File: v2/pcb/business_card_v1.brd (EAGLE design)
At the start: 89 x 51 mm, 70 parts, among them SW1 SPST_TACT-KMR2

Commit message: business card
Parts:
- moved U$1 0.90 mm to (5.08, 46.4)
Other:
- board text added: "Website: https://kevin.lutzer.ca Email: kevin@lutzer.ca Github: https://github.com/kevinlutzer Linkedin: www.linkedin.com/in/kevin-lutzer"
- board text removed: "Website: https://kevin.lutzer.ca Email: kevin@lutzer.ca Github: https://github.com/kevinlutzer"
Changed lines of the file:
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@@
 <dimension x1="0" y1="51.79" x2="89" y2="51.79" x3="44.5" y3="56.79" textsize="1" layer="1"/>
 <dimension x1="89" y1="51.79" x2="89" y2="0.79" x3="94" y3="26.29" textsize="1" layer="1"/>
-<text x="8.89" y="47.625" size="1.778" layer="121">v2</text>
-<text x="8.89" y="45.085" size="1.778" layer="121">Kevin Lutzer</text>
-<text x="1.905" y="40.005" size="1.778" layer="121">B.E. Electrical Engineering &amp;
+<text x="9.525" y="47.625" size="1.778" layer="121">v2</text>
+<text x="9.525" y="45.085" size="1.778" layer="121">Kevin Lutzer</text>
+<text x="2.54" y="39.37" size="1.524" layer="121">B.E. Electrical Engineering &amp;
 B.Sc. Computer Science</text>
-<text x="1.905" y="32.385" size="1.778" layer="121">Website: https://kevin.lutzer.ca
+<text x="2.54" y="29.845" size="1.524" layer="121">Website: https://kevin.lutzer.ca
 Email: kevin@lutzer.ca
-Github: https://github.com/kevinlutzer</text>
-<text x="1.905" y="24.13" size="1.778" layer="121">Plug the usb connector into any usb port,
-and watch! Project details can be found
-  at https://bit.ly/38gpalY.</text>
+Github: https://github.com/kevinlutzer
+Linkedin: www.linkedin.com/in/kevin-lutzer</text>
+<text x="2.54" y="22.86" size="1.524" layer="121">Plug the usb connector into any usb port,
+  and watch! Project details can be found
+      at https://bit.ly/38gpalY.</text>
 </plain>
 <attributes>
@@
 <attribute name="VALUE" x="38.6715" y="12.3825" size="1.27" layer="27" ratio="10" rot="R270"/>
 </element>
-<element name="U$1" library="adafruit" library_urn="urn:adsk.eagle:library:420" package="OSHWLOGO_TOP_0.2" package3d_urn="urn:adsk.eagle:package:6240813/1" value="" x="4.445" y="46.99" smashed="yes"/>
+<element name="U$1" library="adafruit" library_urn="urn:adsk.eagle:library:420" package="OSHWLOGO_TOP_0.2" package3d_urn="urn:adsk.eagle:package:6240813/1" value="" x="5.08" y="46.355" smashed="yes"/>
 </elements>
 <signals>
@@
 <contactref element="IC1" pad="14"/>
 <polygon width="0.6096" layer="16">
-<vertex x="3.175" y="22.86"/>
-<vertex x="45.72" y="22.86"/>
+<vertex x="6.35" y="19.685"/>
+<vertex x="45.72" y="19.685"/>
 <vertex x="45.72" y="0"/>
 <vertex x="26.035" y="0"/>
@@
 <wire x1="17.864746875" y1="12.915" x2="34.29" y2="12.915" width="0.6096" layer="1"/>
 <polygon width="0.6096" layer="1">
-<vertex x="3.175" y="22.86"/>
-<vertex x="45.72" y="22.86"/>
+<vertex x="6.35" y="19.685"/>
+<vertex x="45.72" y="19.685"/>
 <vertex x="45.72" y="0"/>
 <vertex x="26.035" y="0"/>

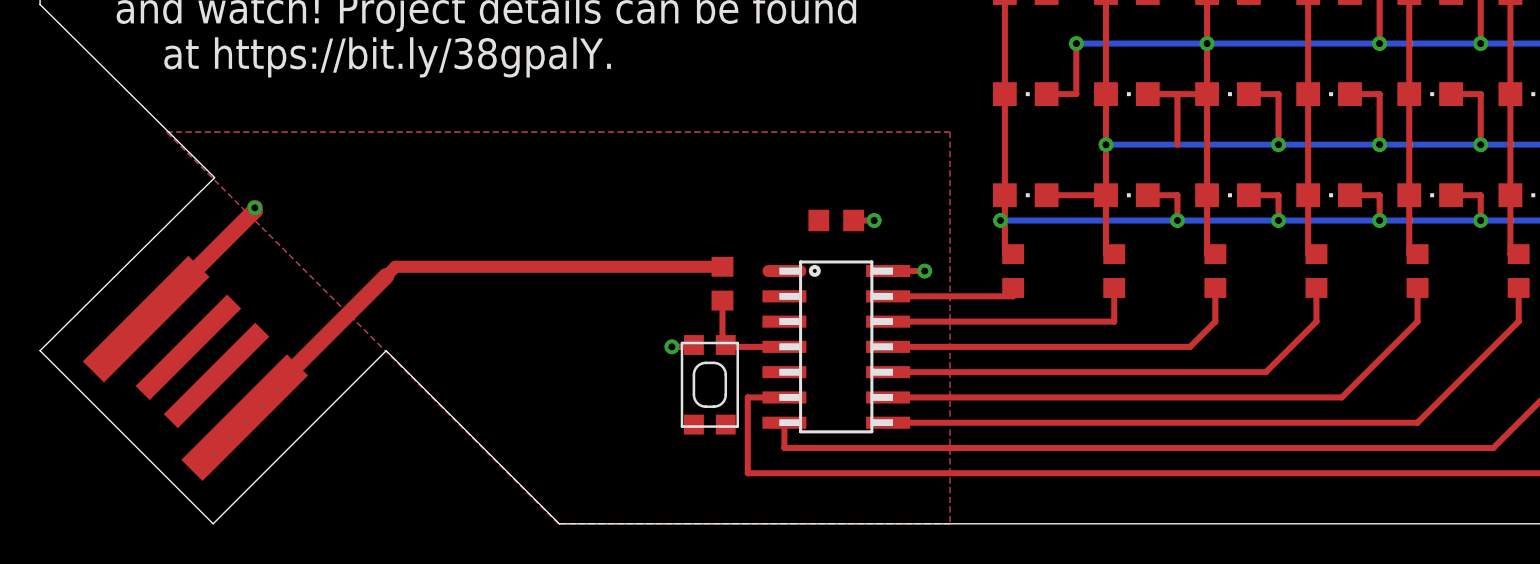
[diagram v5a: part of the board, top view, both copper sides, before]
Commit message: get the business card design done, looking for review now
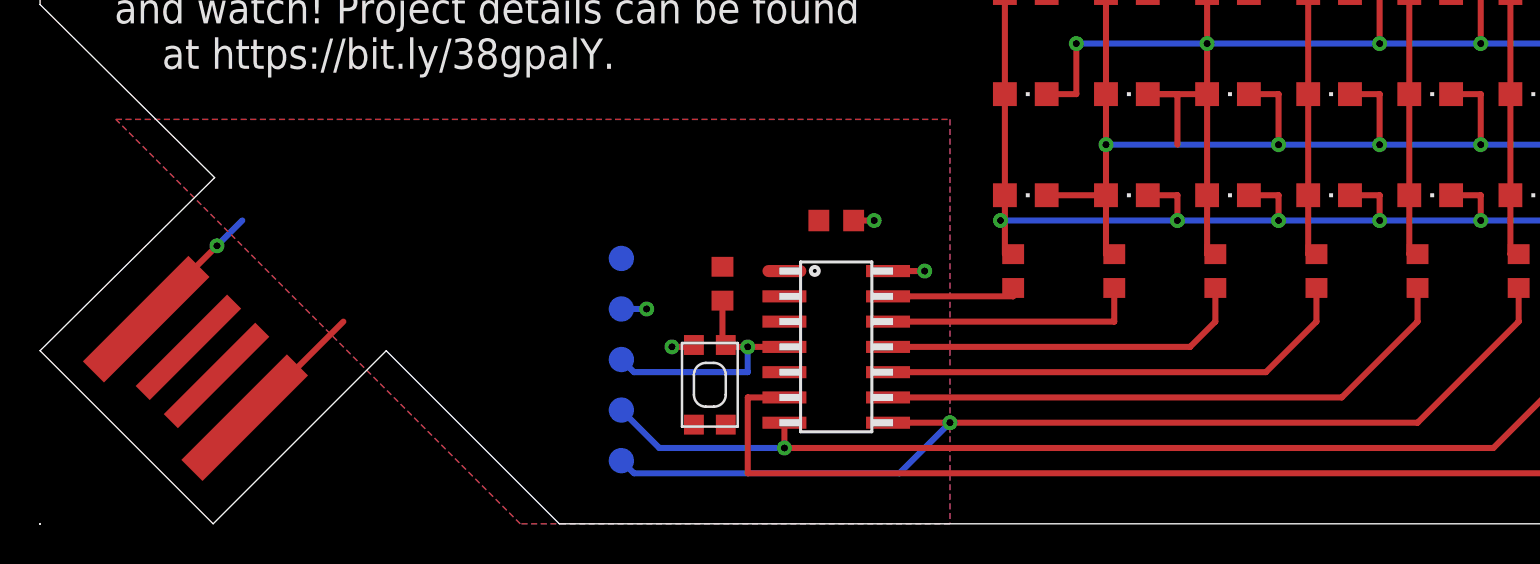
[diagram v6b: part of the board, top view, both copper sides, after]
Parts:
- added TP1, TP2, TP3, TP4, TP5: TEST-POINT3X5, SparkFun-Connectors:PAD.03X.05
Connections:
- net GND: now also TP5.P$1
- net PIN5: now also TP2.P$1
- net PIN6: now also TP4.P$1
- net RESET: now also TP1.P$1
- net UCC: now also TP3.P$1
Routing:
- net UCC: track 27.3 -> 8.39 mm, vias 0 -> 1
- net PIN5: track 35.5 -> 53.3 mm, vias 0 -> 1
- net PIN6: track 47.6 -> 56.6 mm, vias 0 -> 1
- net RESET: track 5.28 -> 13.2 mm, vias 0 -> 1
- net GND: track 12.0 -> 11.0 mm

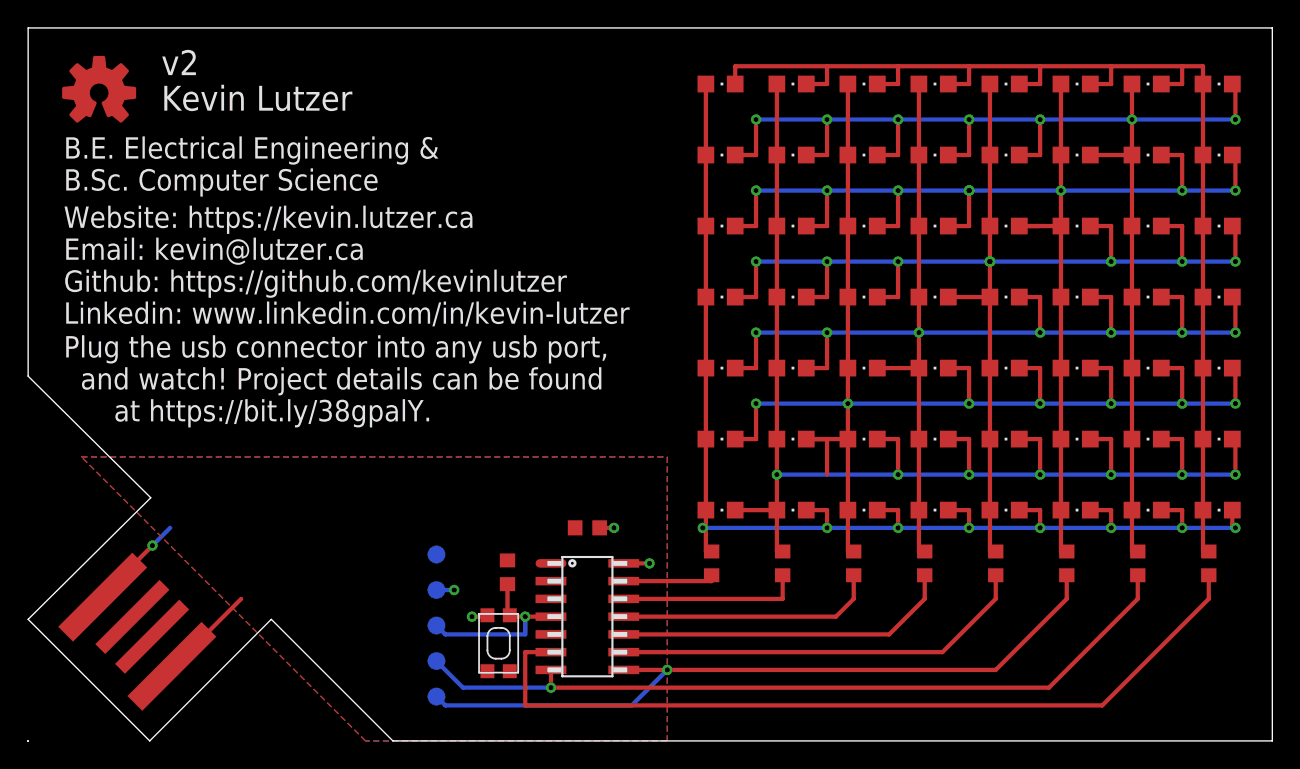
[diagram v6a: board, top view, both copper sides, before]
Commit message: fix some of the silk screen
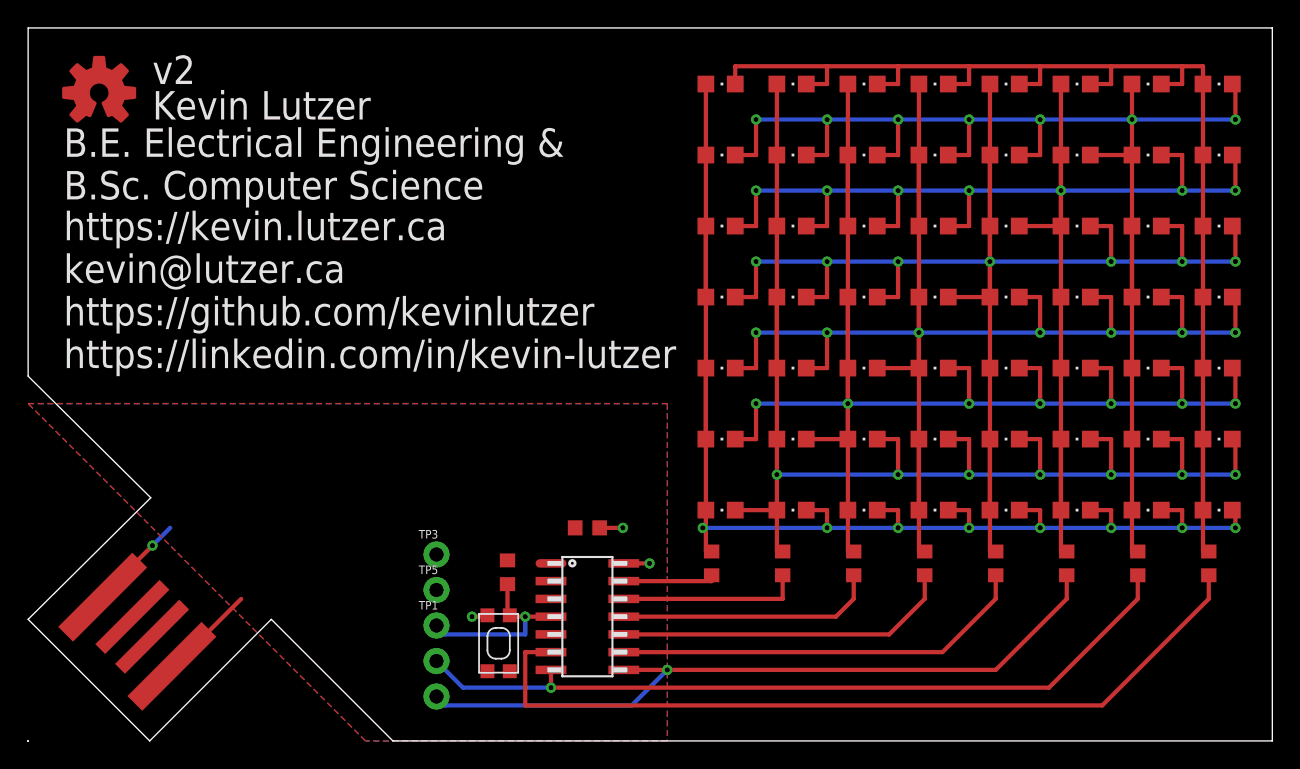
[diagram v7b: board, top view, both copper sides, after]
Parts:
- TP1, TP2, TP3, TP4, TP5: value TEST-POINT3X5 -> TEST-POINTPOGO_PTH; device SparkFun-Connectors:PAD.03X.05 -> SparkFun-Connectors:1X01_NO_SILK
- moved TP3 2.54 mm to (29.2, 13.3), flipped to the top, turned to 0 degrees
- moved TP5 2.54 mm to (29.2, 10.8), flipped to the top
- flipped TP1 to the top
- flipped TP2 to the top
- flipped TP4 to the top
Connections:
- net GND: now also TP5.1; no longer TP5.P$1
- net PIN5: now also TP2.1; no longer TP2.P$1
- net PIN6: now also TP4.1; no longer TP4.P$1
- net RESET: now also TP1.1; no longer TP1.P$1
- net UCC: now also TP3.1; no longer TP3.P$1
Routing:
- net N$34: track 94.0 -> 109.3 mm, vias 8 -> 7
- net N$4: track 94.0 -> 109.3 mm
- net N$3: track 98.1 -> 109.3 mm
- net N$1: track 90.1 -> 100.3 mm
- net N$31: track 95.5 -> 104.2 mm, vias 8 -> 7
- net N$8: track 86.4 -> 91.5 mm
- net N$15: track 94.0 -> 99.1 mm
- net N$2: track 92.5 -> 97.6 mm
- net UCC: track 8.39 -> 6.83 mm, vias 1 -> 0
- net GND: track 11.0 -> 11.6 mm
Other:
- board text added: "Plug the usb connector into any usb port, and watch! Project details can be found at https://bit.ly/38gpalY"
- board text added: "https://kevin.lutzer.ca kevin@lutzer.ca https://github.com/kevinlutzer https://linkedin.com/in/kevin-lutzer"
- board text removed: "Plug the usb connector into any usb port, and watch! Project details can be found at https://bit.ly/38gpalY."
- board text removed: "Website: https://kevin.lutzer.ca Email: kevin@lutzer.ca Github: https://github.com/kevinlutzer Linkedin: www.linkedin.com/in/kevin-lutzer"
